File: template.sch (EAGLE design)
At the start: 5 parts

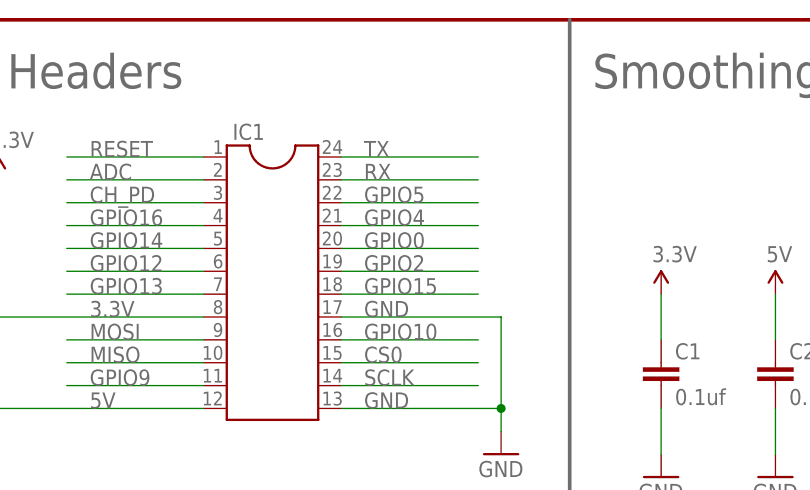
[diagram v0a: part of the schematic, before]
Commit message: Renamed GPIO4 & GPIO5 as SDA and SCL respectively to suit their default i2c states.
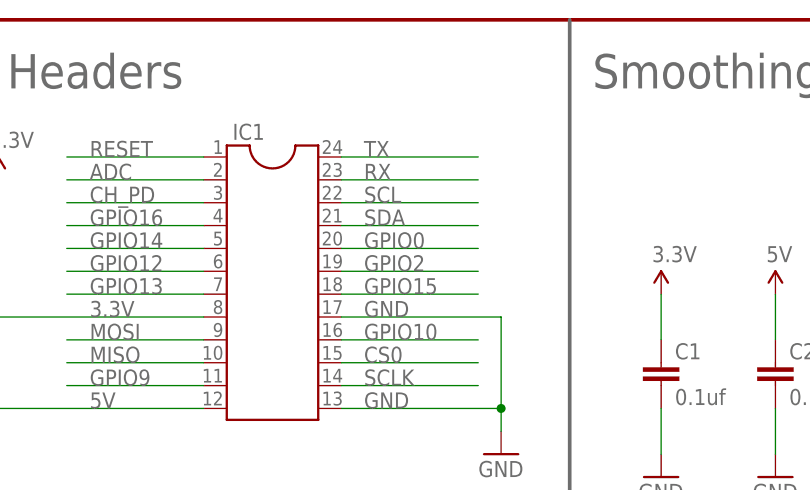
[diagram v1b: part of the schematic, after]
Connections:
- net GPIO4 renamed SDA
- net GPIO5 renamed SCL
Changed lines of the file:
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@@
 </segment>
 </net>
-<net name="GPIO4" class="0">
+<net name="SDA" class="0">
 <segment>
 <pinref part="IC1" gate="G$1" pin="21"/>
@@
 </segment>
 </net>
-<net name="GPIO5" class="0">
+<net name="SCL" class="0">
 <segment>
 <pinref part="IC1" gate="G$1" pin="22"/>
